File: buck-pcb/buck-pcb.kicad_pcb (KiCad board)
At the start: 2 copper layers, 50 x 50 mm, 38 parts, among them J1 Conn_01x02, J2 Conn_01x02, Q1 Q_PMOS_GSD, Q2 MMBT3906, Q3 BSS123, Q4 MMBT3906, Q5 MMBT3906, U1 LM393, U2 LMC6482

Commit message: Initial layout
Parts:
- added C10: 0.1u, Capacitor_SMD:C_0603_1608Metric, F.Cu at (104.1, 91.9)
- added Ref**: Val**, buck-graphics:pcb-inkscape, F.Cu at (119.8, 89.9)
- D2: footprint Diode_THT:D_DO-41_SOD81_P7.62mm_Horizontal -> Diode_SMD:D_SOD-123
- L1: footprint Inductor_SMD:L_7.3x7.3_H3.5 -> buck-graphics:BMRx00060630
- moved D4 40.9 mm to (137.2, 79.2), turned to -90 degrees
- moved D2 38.5 mm to (134.9, 91.8), turned to -90 degrees
- moved J2 34.7 mm to (140.0, 73.0)
- moved C5 32.9 mm to (130.8, 72.5), turned to -90 degrees
- moved Q2 30.9 mm to (104.7, 78.8), turned to 180 degrees
- moved R2 29.7 mm to (104.1, 89.9)
- moved R3 25.3 mm to (112.3, 87.6), turned to 180 degrees
- moved Q1 24.3 mm to (107.4, 71.6)
- moved C1 22.0 mm to (103.6, 74.4), turned to -90 degrees
- moved J1 20.5 mm to (100.0, 73.0)
- moved L1 20.4 mm to (121.4, 73.2)
- moved R4 19.9 mm to (104.7, 82.1), turned to 180 degrees
- moved R1 19.8 mm to (107.4, 89.9)
- moved U1 18.0 mm to (118.9, 82.0)
- moved D1 17.4 mm to (108.8, 78.8), turned to 90 degrees
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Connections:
- net Net-(C5-Pad1) renamed /VOUT
- net Net-(D3-Pad1) renamed /VSW
- U2 pad 1: Net-(C3-Pad1) -> Net-(C2-Pad2)
- U2 pad 2: Net-(C3-Pad2) -> Net-(C2-Pad1)
- U2 pad 3: /Vref_5 -> /Vref_MID
- U2 pad 5: /Vref_MID -> /Vref_5
- U2 pad 6: Net-(C2-Pad1) -> Net-(C3-Pad2)
- U2 pad 7: Net-(C2-Pad2) -> Net-(C3-Pad1)
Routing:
- net /VIN: track 0.00 -> 81.0 mm, vias 0 -> 3
- net /Vref_MID: track 0.00 -> 28.0 mm
- net Net-(C3-Pad1): track 0.00 -> 25.7 mm, vias 0 -> 3
- net Net-(R14-Pad2): track 0.00 -> 19.8 mm, vias 0 -> 2
- net /VOUT: track 0.00 -> 19.3 mm
- net Net-(R5-Pad1): track 0.00 -> 18.5 mm, vias 0 -> 2
- net /Vref_5: track 0.00 -> 17.5 mm
- net Net-(R6-Pad1): track 0.00 -> 15.6 mm
- net Net-(C3-Pad2): track 0.00 -> 15.2 mm
- net Net-(C2-Pad2): track 0.00 -> 13.9 mm
- net Net-(D1-Pad2): track 0.00 -> 11.4 mm
- net Net-(D1-Pad1): track 0.00 -> 9.46 mm
- net Net-(C2-Pad1): track 0.00 -> 7.21 mm
- net Net-(Q4-Pad1): track 0.00 -> 6.91 mm
- net Net-(Q4-Pad2): track 0.00 -> 5.07 mm
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- added copper zone on F.Cu, net /VIN
- added copper zone on F.Cu, net /VOUT
- added copper zone on F.Cu, net /VSW
- added copper zone on B.Cu, net GND
- added copper zone on F.Cu, net GND

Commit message: Working on layout
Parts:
- moved R8 2.54 mm to (118.1, 87.6)
- moved R3 1.02 mm to (113.3, 87.6)
- moved C2 0.56 mm to (113.3, 89.4)
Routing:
- net Net-(R6-Pad1): track 15.6 -> 8.57 mm
- net Net-(R14-Pad2): track 19.8 -> 17.4 mm
- net GND: vias 20 -> 50
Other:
- board text added: "Compensator"
- board text added: "Gate Driver"
- board text added: "Input 7-12V"
- board text added: "Output 5V"
- board text added: "PWM"
- board text added: "Ramp Gen"
- board text added: "Vref Gen"

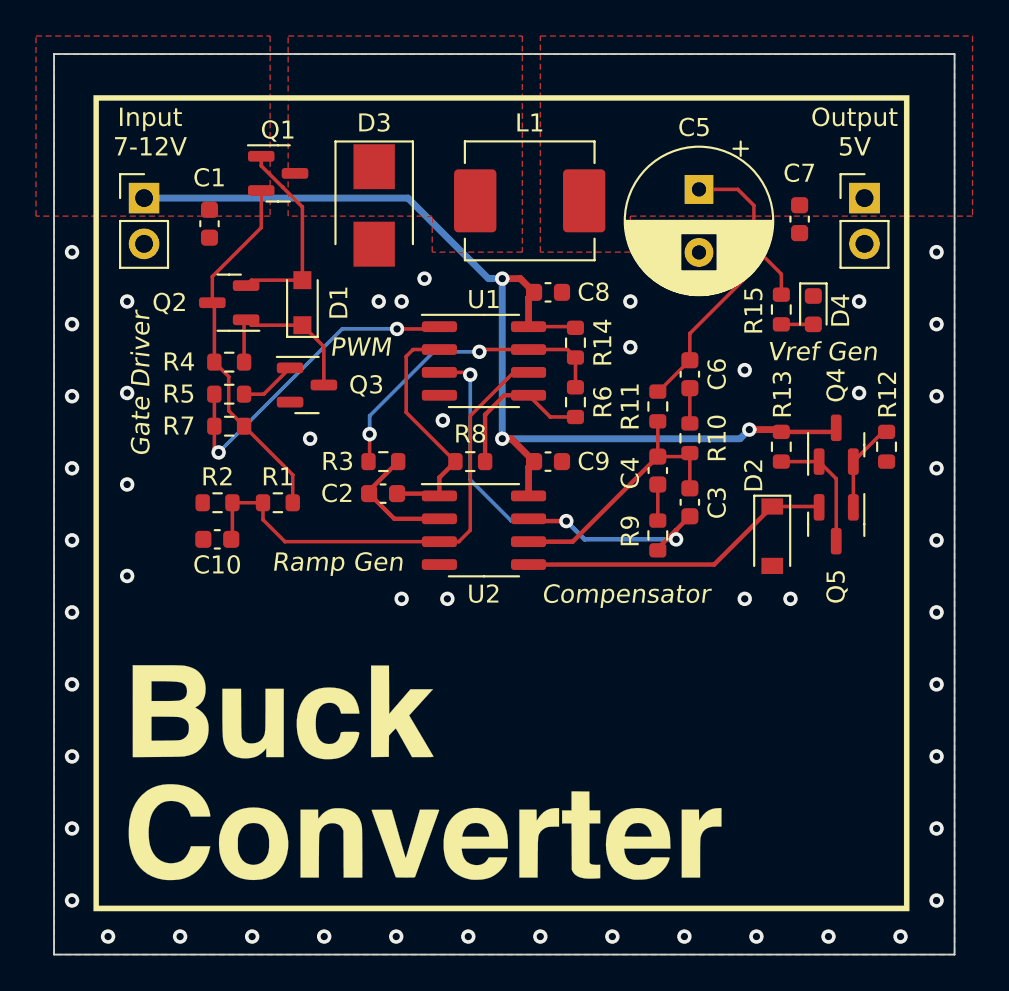
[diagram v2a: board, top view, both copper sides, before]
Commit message: Added more PCB art
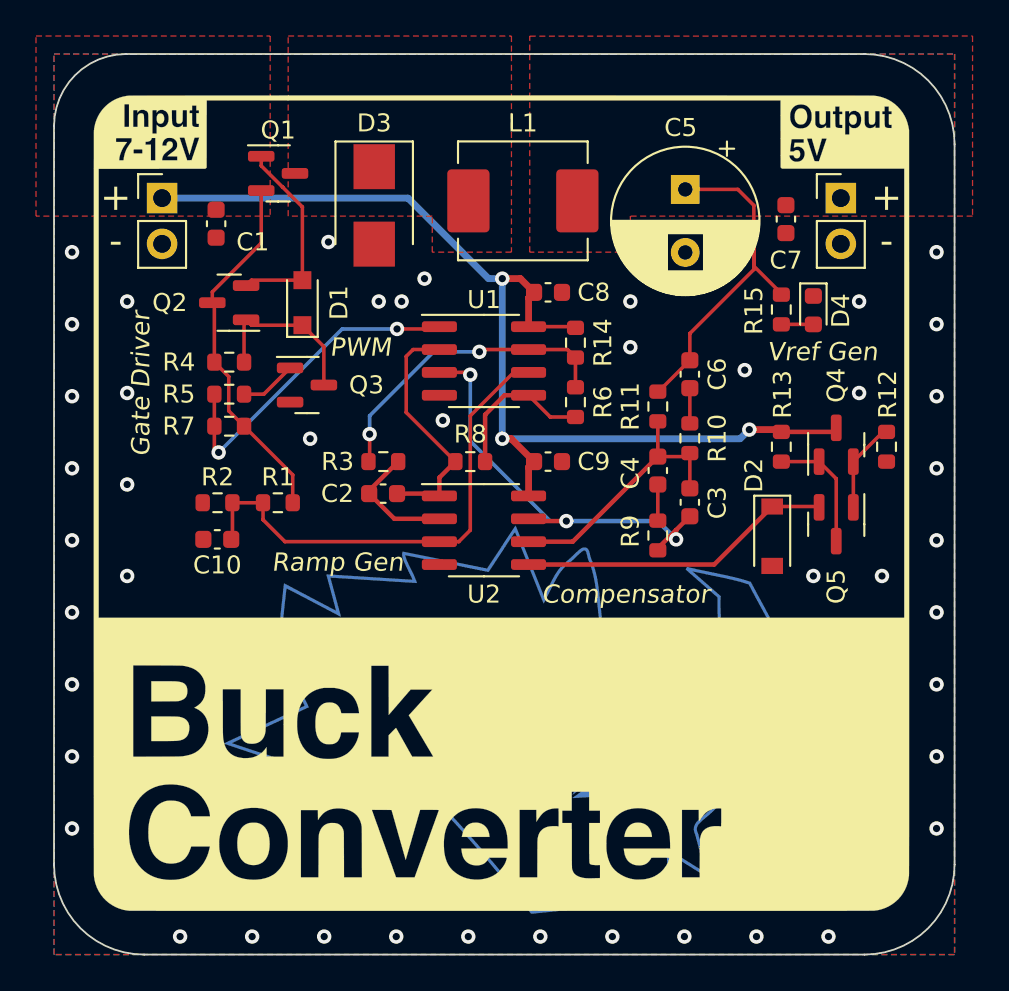
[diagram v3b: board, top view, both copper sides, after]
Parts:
- added REF**: MountingHole_3.2mm_M3_ISO7380_Pad, MountingHole:MountingHole_3.2mm_M3_ISO7380_Pad, F.Cu at (138.7, 108.7)
- added Ref**: Val**, buck-graphics:pcb-art-back, B.Cu at (119.9, 102.1)
- moved J2 1.32 mm to (138.7, 73.0)
- moved J1 1.00 mm to (101.0, 73.0)
- moved C5 0.76 mm to (130.0, 72.5)
- moved C7 0.76 mm to (135.6, 74.2)
- moved L1 0.38 mm to (121.0, 73.2)
- moved C1 0.37 mm to (104.0, 74.4)
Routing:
- net Net-(C3-Pad1): track 25.7 -> 24.4 mm
- net /VIN: track 81.0 -> 80.0 mm
- net GND: vias 50 -> 45
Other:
- outline, holes or cut-outs redrawn
- board text added: "+ -"
- board text added: "Jeffrey Ni 2022"
- board text removed: "Input 7-12V"
- board text removed: "Output 5V"

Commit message: Gerbers sent
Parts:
- added TP1: TestPoint, TestPoint:TestPoint_Keystone_5005-5009_Compact, F.Cu at (99.9, 91.4)
- C5: footprint Capacitor_THT:CP_Radial_D8.0mm_P3.50mm -> Capacitor_SMD:CP_Elec_6.3x4.9
- moved C5 1.57 mm to (129.7, 74.0)
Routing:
- net Net-(C2-Pad2): track 14.2 -> 13.7 mm
- net /VOUT: track 19.3 -> 19.9 mm
- net GND: vias 45 -> 44
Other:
- board text added: "GND"
